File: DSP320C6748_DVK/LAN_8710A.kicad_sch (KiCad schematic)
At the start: 56 parts, among them J12 RJ45_Halo_HFJ11-x2450E-LxxRL, U7 LAN8710A, Y6 25MHz

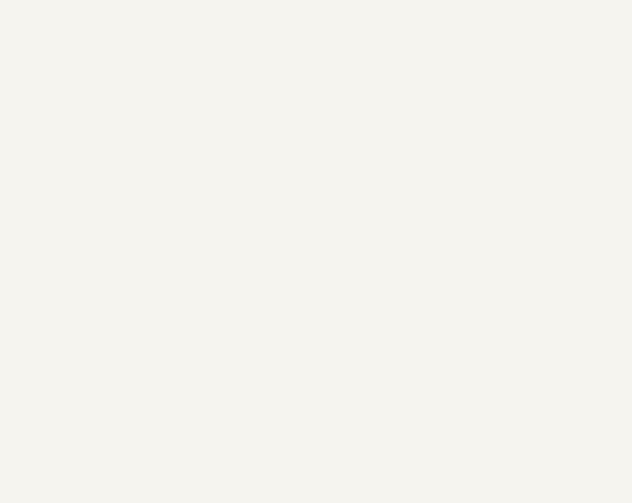
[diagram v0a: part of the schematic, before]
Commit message: Connectors and mislleneous components added
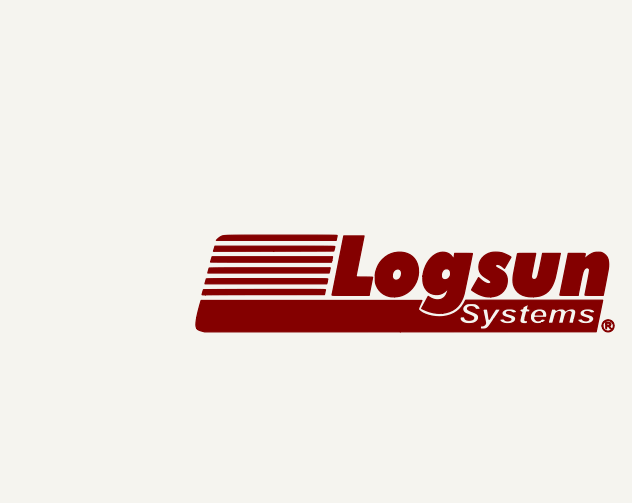
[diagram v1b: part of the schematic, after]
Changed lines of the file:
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@@
+	)
+	(symbol
+		(lib_id "Logsun_Logo:LOGO")
+		(at 260.35 173.99 0)
+		(unit 1)
+		(body_style 1)
+		(exclude_from_sim no)
+		(in_bom yes)
+		(on_board yes)
+		(in_pos_files yes)
+		(dnp no)
+		(fields_autoplaced yes)
+		(property "Reference" "#G13"
+			(at 260.35 168.025 0)
+			(hide yes)
+			(show_name no)
+			(do_not_autoplace no)
+			(effects
+				(font
+					(size 1.27 1.27)
+				)
+			)
+		)
+		(property "Value" "LOGO"
+			(at 260.35 179.955 0)
+			(hide yes)
+			(show_name no)
+			(do_not_autoplace no)
+			(effects
+				(font
+					(size 1.27 1.27)
+				)
+			)
+		)
+		(property "Footprint" ""
+			(at 260.35 173.99 0)
+			(hide yes)
+			(show_name no)
+			(do_not_autoplace no)
+			(effects
+				(font
+					(size 1.27 1.27)
+				)
+			)
+		)
+		(property "Datasheet" ""
+			(at 260.35 173.99 0)
+			(hide yes)
+			(show_name no)
+			(do_not_autoplace no)
+			(effects
+				(font
+					(size 1.27 1.27)
+				)
+			)
+		)
+		(property "Description" ""
+			(at 260.35 173.99 0)
+			(hide yes)
+			(show_name no)
+			(do_not_autoplace no)
+			(effects
+				(font
+					(size 1.27 1.27)
+				)
+			)
+		)
+		(instances
+			(project "DSP320C6748_DVK"
+				(path "/3a70ffc0-9fe7-4a5b-b3c2-23140355df82/6c2ac236-d8bd-4367-9643-603071189f95"
+					(reference "#G13")
+					(unit 1)
+				)
+			)
+		)
 	)
 	(symbol

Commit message: Whole Schematic Reannotation Done
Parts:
- renumbered C184 to C191, C185 to C192, C186 to C193, C187 to C194, C188 to C195, C189 to C196, C181 to C197, C190 to C198, C182 to C199, C191 to C200, C183 to C201, C192 to C202, FB13 to FB14, R210 to R184, R211 to R185, R226 to R186, R212 to R187, R227 to R188, R221 to R189, R215 to R190, R214 to R191, R213 to R192, R216 to R193, R217 to R194, R218 to R195, R219 to R196, R220 to R197, R228 to R198, R229 to R199, R234 to R200, R230 to R201, R233 to R202, R231 to R203, R232 to R204, R223 to R205, R225 to R206, R224 to R207, R222 to R208, R241 to R209, R242 to R210, R235 to R211, R236 to R212, R237 to R213, R238 to R214, R239 to R215, R240 to R216, R243 to R217, R244 to R218, R245 to R219, R246 to R220, R247 to R221, R248 to R222, TP11 to TP18, U7 to U10

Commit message: Schematic Corrections-II Done
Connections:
- net ENET_RXN: now also C198.1, R217.1
- net ENET_RXP: now also C200.1, R218.1
- net ENET_TXN: no longer C198.1, R217.1
- net ENET_TXP: no longer C200.1, R218.1
- net UARTO_RX: now also R216.1
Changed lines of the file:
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@@
+	(wire
+		(pts
+			(xy 128.27 186.69) (xy 133.35 186.69)
+		)
+		(stroke
+			(width 0)
+			(type default)
+		)
+	)
 	(wire
 		(pts
@@
 		)
 	)
-	(label "ENET_TXN"
-		(at 175.26 48.26 180)
-		(effects
-			(font
-				(size 1.27 1.27)
-			)
-			(justify right bottom)
-		)
-	)
 	(label "LINK_LED"
 		(at 265.43 97.79 180)
@@
 		)
 	)
+	(label "ENET_RXN"
+		(at 175.26 48.26 180)
+		(effects
+			(font
+				(size 1.27 1.27)
+			)
+			(justify right bottom)
+		)
+	)
 	(label "ACT_LED"
 		(at 110.49 71.12 180)
@@
 		)
 	)
-	(label "ENET_TXP"
+	(label "ENET_RXP"
 		(at 175.26 45.72 180)
 		(effects

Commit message: DC jack Replaced With Type-C, ADC and RTC section added
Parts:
- renumbered C191 to C193, C192 to C194, C193 to C195, C194 to C196, C195 to C197, C196 to C198, C197 to C199, C198 to C200, C199 to C201, C200 to C202, C201 to C203, C202 to C204, FB14 to FB16, J12 to J13, R184 to R188, R185 to R189, R186 to R190, R187 to R191, R188 to R192, R189 to R193, R190 to R194, R191 to R195, R192 to R196, R193 to R197, R194 to R198, R195 to R199, R196 to R200, R197 to R201, R198 to R202, R199 to R203, R200 to R204, R201 to R205, R202 to R206, R203 to R207, R204 to R208, R205 to R209, R206 to R210, R207 to R211, R208 to R212, R209 to R213, R210 to R214, R211 to R215, R212 to R216, R213 to R217, R214 to R218, R215 to R219, R216 to R220, R217 to R221, R218 to R222, R219 to R223, R220 to R224, R221 to R225, R222 to R226

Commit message: Scheamtic Re-annotation done, Some footprints assigned
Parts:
- C196: renamed from C193; footprint (none) -> Capacitor_SMD:C_0603_1608Metric_Pad1.08x0.95mm_HandSolder
- C197: renamed from C194; footprint (none) -> Capacitor_SMD:C_0603_1608Metric_Pad1.08x0.95mm_HandSolder
- C198: renamed from C195; footprint (none) -> Capacitor_SMD:C_0603_1608Metric_Pad1.08x0.95mm_HandSolder
- C199: renamed from C196; footprint (none) -> Capacitor_SMD:C_0603_1608Metric_Pad1.08x0.95mm_HandSolder
- C200: renamed from C197; footprint (none) -> Capacitor_SMD:C_0603_1608Metric_Pad1.08x0.95mm_HandSolder
- C201: renamed from C198; footprint (none) -> Capacitor_SMD:C_0603_1608Metric_Pad1.08x0.95mm_HandSolder
- C202: renamed from C199; footprint (none) -> Capacitor_SMD:C_0603_1608Metric_Pad1.08x0.95mm_HandSolder
- C203: renamed from C200; footprint (none) -> Capacitor_SMD:C_0603_1608Metric_Pad1.08x0.95mm_HandSolder
- C204: renamed from C201; footprint (none) -> Capacitor_SMD:C_0603_1608Metric_Pad1.08x0.95mm_HandSolder
- C205: renamed from C202; footprint (none) -> Capacitor_SMD:C_0603_1608Metric_Pad1.08x0.95mm_HandSolder
- C206: renamed from C203; footprint (none) -> Capacitor_SMD:C_0603_1608Metric_Pad1.08x0.95mm_HandSolder
- C207: renamed from C204; footprint (none) -> Capacitor_SMD:C_0603_1608Metric_Pad1.08x0.95mm_HandSolder
- FB17: renamed from FB16; footprint (none) -> Inductor_SMD:L_0805_2012Metric_Pad1.05x1.20mm_HandSolder
- R190: renamed from R188; footprint (none) -> Resistor_SMD:R_0603_1608Metric_Pad0.98x0.95mm_HandSolder
- R191: renamed from R189; footprint (none) -> Resistor_SMD:R_0603_1608Metric_Pad0.98x0.95mm_HandSolder
- R192: renamed from R190; footprint (none) -> Resistor_SMD:R_0603_1608Metric_Pad0.98x0.95mm_HandSolder
- R193: renamed from R191; footprint (none) -> Resistor_SMD:R_0603_1608Metric_Pad0.98x0.95mm_HandSolder
- R194: renamed from R192; footprint (none) -> Resistor_SMD:R_0603_1608Metric_Pad0.98x0.95mm_HandSolder
- R195: renamed from R193; footprint (none) -> Resistor_SMD:R_0603_1608Metric_Pad0.98x0.95mm_HandSolder
- R196: renamed from R194; footprint (none) -> Resistor_SMD:R_0603_1608Metric_Pad0.98x0.95mm_HandSolder
- R197: renamed from R195; footprint (none) -> Resistor_SMD:R_0603_1608Metric_Pad0.98x0.95mm_HandSolder
- R198: renamed from R196; footprint (none) -> Resistor_SMD:R_0603_1608Metric_Pad0.98x0.95mm_HandSolder
- R199: renamed from R197; footprint (none) -> Resistor_SMD:R_0603_1608Metric_Pad0.98x0.95mm_HandSolder
- R200: renamed from R198; footprint (none) -> Resistor_SMD:R_0603_1608Metric_Pad0.98x0.95mm_HandSolder
- R201: renamed from R199; footprint (none) -> Resistor_SMD:R_0603_1608Metric_Pad0.98x0.95mm_HandSolder
- R202: renamed from R200; footprint (none) -> Resistor_SMD:R_0603_1608Metric_Pad0.98x0.95mm_HandSolder
- R203: renamed from R201; footprint (none) -> Resistor_SMD:R_0603_1608Metric_Pad0.98x0.95mm_HandSolder
- R204: renamed from R202; footprint (none) -> Resistor_SMD:R_0603_1608Metric_Pad0.98x0.95mm_HandSolder
- R205: renamed from R203; footprint (none) -> Resistor_SMD:R_0603_1608Metric_Pad0.98x0.95mm_HandSolder
- R206: renamed from R204; footprint (none) -> Resistor_SMD:R_0603_1608Metric_Pad0.98x0.95mm_HandSolder
- R207: renamed from R205; footprint (none) -> Resistor_SMD:R_0603_1608Metric_Pad0.98x0.95mm_HandSolder
- R208: renamed from R206; footprint (none) -> Resistor_SMD:R_0603_1608Metric_Pad0.98x0.95mm_HandSolder
- R209: renamed from R207; footprint (none) -> Resistor_SMD:R_0603_1608Metric_Pad0.98x0.95mm_HandSolder
- R210: renamed from R208; footprint (none) -> Resistor_SMD:R_0603_1608Metric_Pad0.98x0.95mm_HandSolder
- R211: renamed from R209; footprint (none) -> Resistor_SMD:R_0603_1608Metric_Pad0.98x0.95mm_HandSolder
- R212: renamed from R210; footprint (none) -> Resistor_SMD:R_0603_1608Metric_Pad0.98x0.95mm_HandSolder
- R213: renamed from R211; footprint (none) -> Resistor_SMD:R_0603_1608Metric_Pad0.98x0.95mm_HandSolder
- R214: renamed from R212; footprint (none) -> Resistor_SMD:R_0603_1608Metric_Pad0.98x0.95mm_HandSolder
- R215: renamed from R213; footprint (none) -> Resistor_SMD:R_0603_1608Metric_Pad0.98x0.95mm_HandSolder
- R216: renamed from R214; footprint (none) -> Resistor_SMD:R_0603_1608Metric_Pad0.98x0.95mm_HandSolder
- R217: renamed from R215; footprint (none) -> Resistor_SMD:R_0603_1608Metric_Pad0.98x0.95mm_HandSolder
- R218: renamed from R216; footprint (none) -> Resistor_SMD:R_0603_1608Metric_Pad0.98x0.95mm_HandSolder
- R219: renamed from R217; footprint (none) -> Resistor_SMD:R_0603_1608Metric_Pad0.98x0.95mm_HandSolder
- R220: renamed from R218; footprint (none) -> Resistor_SMD:R_0603_1608Metric_Pad0.98x0.95mm_HandSolder
- R221: renamed from R219; footprint (none) -> Resistor_SMD:R_0603_1608Metric_Pad0.98x0.95mm_HandSolder
- R222: renamed from R220; footprint (none) -> Resistor_SMD:R_0603_1608Metric_Pad0.98x0.95mm_HandSolder
- R223: renamed from R221; footprint (none) -> Resistor_SMD:R_0603_1608Metric_Pad0.98x0.95mm_HandSolder
- R224: renamed from R222; footprint (none) -> Resistor_SMD:R_0603_1608Metric_Pad0.98x0.95mm_HandSolder
- R225: renamed from R223; footprint (none) -> Resistor_SMD:R_0603_1608Metric_Pad0.98x0.95mm_HandSolder
- R226: renamed from R224; footprint (none) -> Resistor_SMD:R_0603_1608Metric_Pad0.98x0.95mm_HandSolder
- R227: renamed from R225; footprint (none) -> Resistor_SMD:R_0603_1608Metric_Pad0.98x0.95mm_HandSolder
- R228: renamed from R226; footprint (none) -> Resistor_SMD:R_0603_1608Metric_Pad0.98x0.95mm_HandSolder
- TP18: footprint (none) -> TestPoint:TestPoint_Pad_D3.0mm
